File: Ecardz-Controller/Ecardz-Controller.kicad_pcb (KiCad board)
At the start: 4 copper layers, 189 x 115 mm, 169 parts, among them IC1 ST25R3916B-AQWT, IC2 INA180A2IDBVR, J1 MEM2061-01-188-00-A, J10 Conn_01x02, J2 Conn_01x04, J3 Conn_01x05, J4 Conn_01x09, J5 Conn_01x01, J6 Conn_01x24, J7 Conn_01x02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

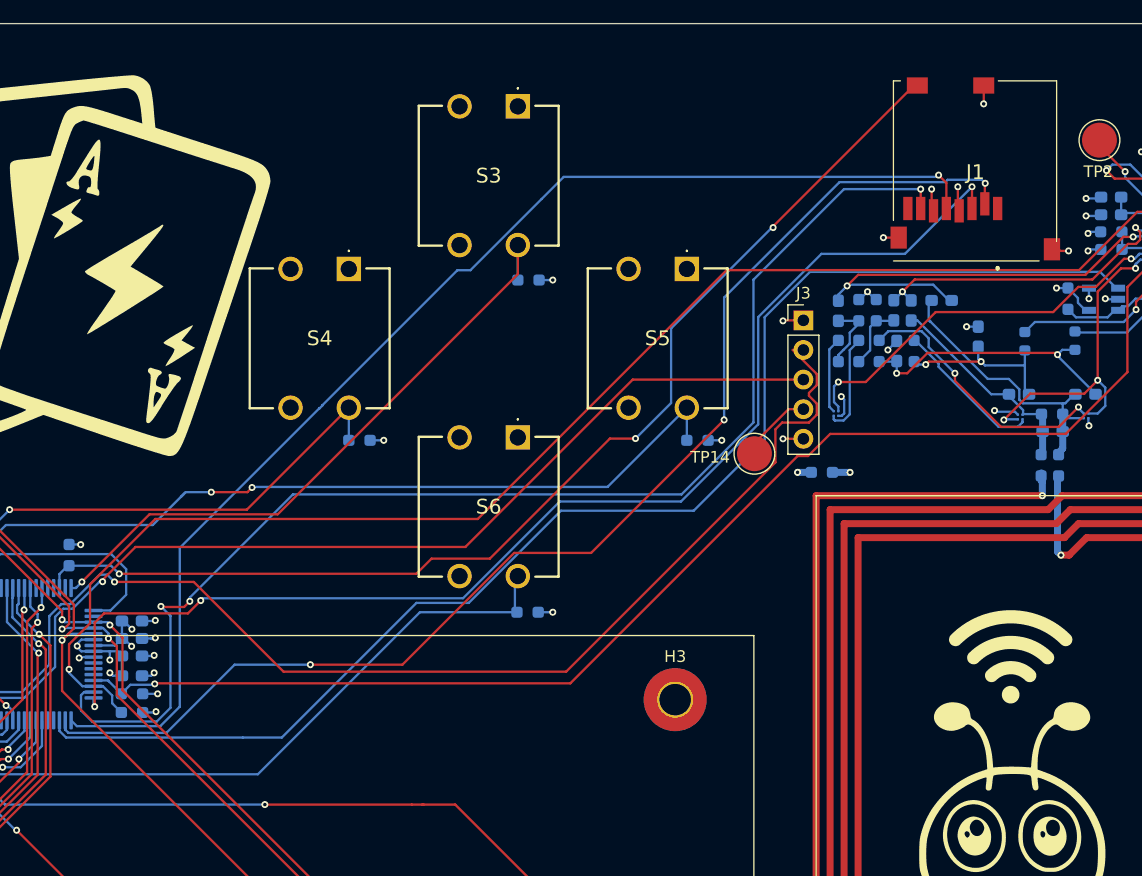
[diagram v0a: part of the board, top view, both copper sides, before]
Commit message: flipped SD card so it enters from card edge
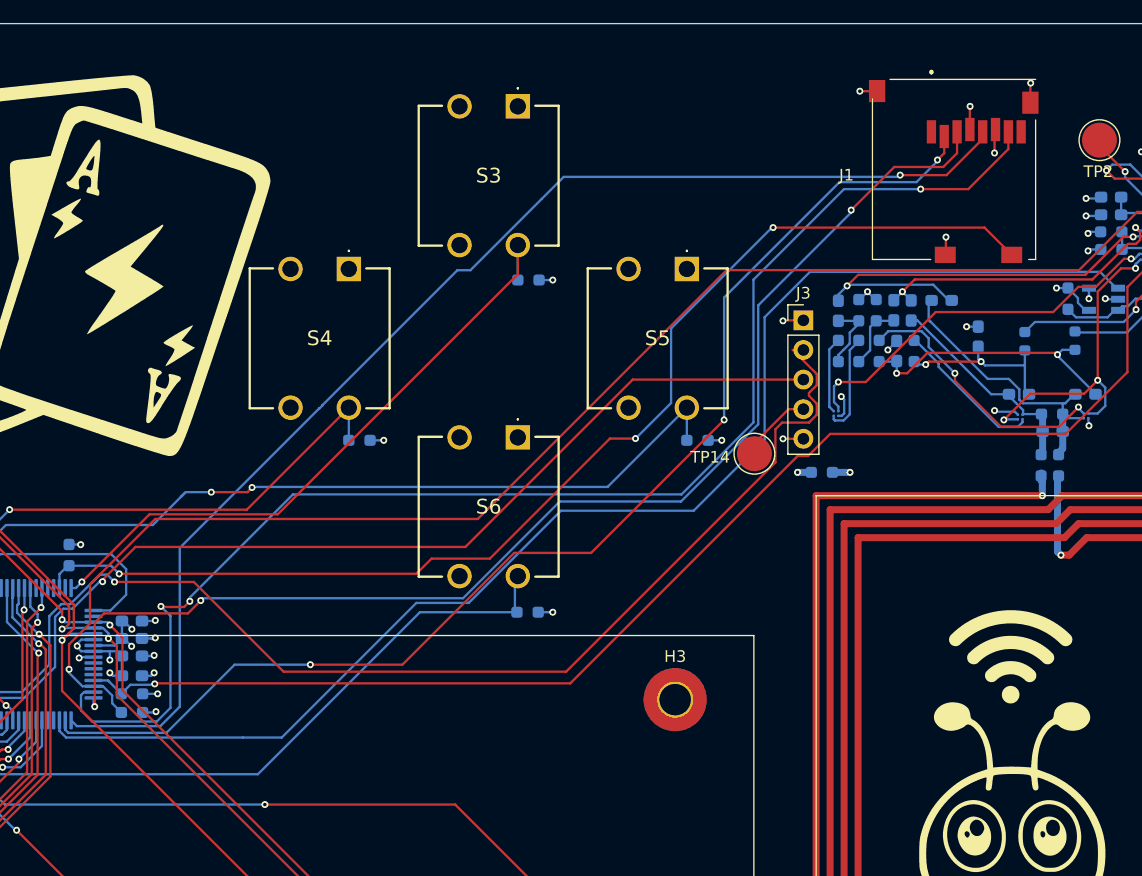
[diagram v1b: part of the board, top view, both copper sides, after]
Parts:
- moved J1 11.7 mm to (205.7, 99.3), turned to 180 degrees
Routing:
- net /MCU/SD_MISO: track 109.2 -> 117.9 mm
- net /MCU/SD_CARD_DETECT: track 96.6 -> 100.7 mm
- net /MCU/SD_SCK: track 104.8 -> 107.9 mm
- net /MCU/SD_CS: track 107.5 -> 104.6 mm
- net /MCU/SD_MOSI: track 105.5 -> 106.6 mm

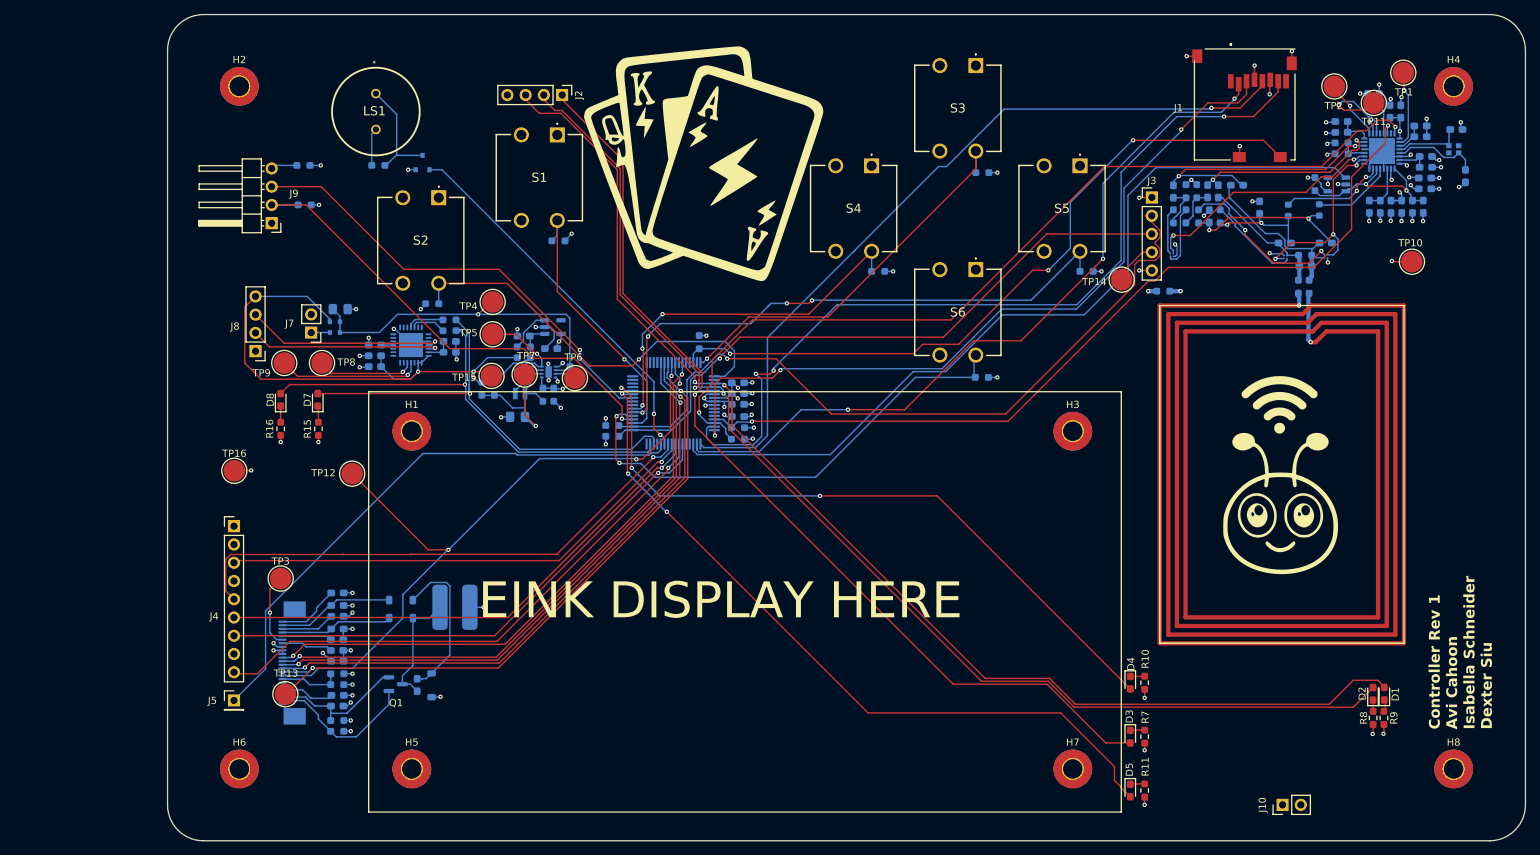
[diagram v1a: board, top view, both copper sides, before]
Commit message: changed headers to 90 degree angled headers
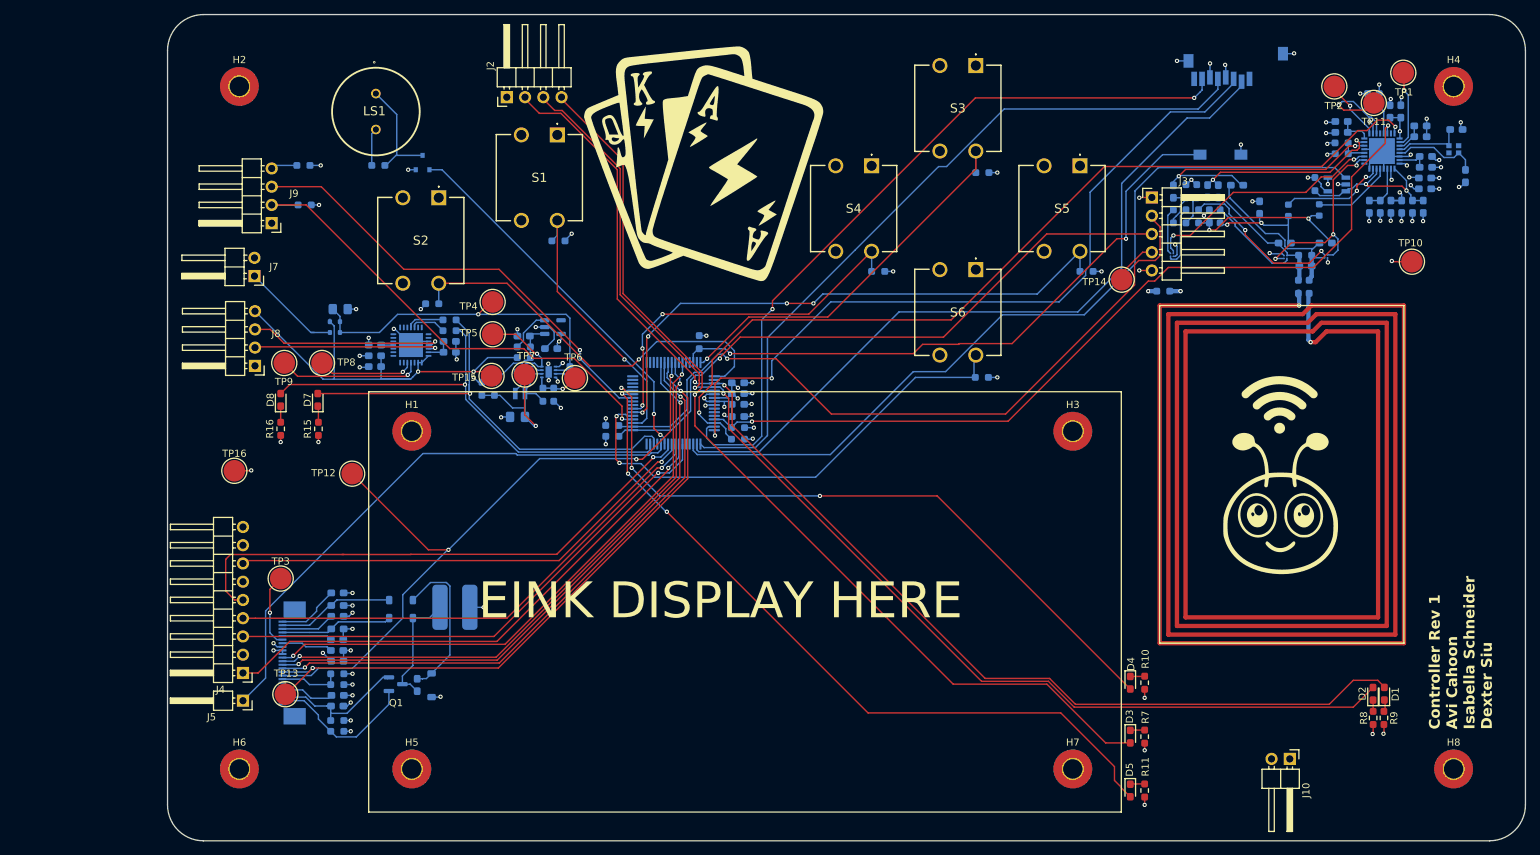
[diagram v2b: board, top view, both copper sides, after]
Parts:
- J1: moved to B.Cu
- J10, J7: footprint Connector_PinHeader_2.54mm:PinHeader_1x02_P2.54mm_Vertical -> Connector_PinHeader_2.54mm:PinHeader_1x02_P2.54mm_Horizontal
- J2, J8: footprint Connector_PinHeader_2.54mm:PinHeader_1x04_P2.54mm_Vertical -> Connector_PinHeader_2.54mm:PinHeader_1x04_P2.54mm_Horizontal
- J3: footprint Connector_PinHeader_2.54mm:PinHeader_1x05_P2.54mm_Vertical -> Connector_PinHeader_2.54mm:PinHeader_1x05_P2.54mm_Horizontal
- J4: footprint Connector_PinHeader_2.54mm:PinHeader_1x09_P2.54mm_Vertical -> Connector_PinHeader_2.54mm:PinHeader_1x09_P2.54mm_Horizontal
- J5: footprint Connector_PinHeader_2.54mm:PinHeader_1x01_P2.54mm_Vertical -> Connector_PinHeader_2.54mm:PinHeader_1x01_P2.54mm_Horizontal
- moved J4 20.5 mm to (60.5, 181.6), turned to 180 degrees
- moved J1 12.8 mm to (192.9, 99.0), turned to 0 degrees
- moved J7 11.2 mm to (62.1, 126.4)
- moved J2 7.71 mm to (97.2, 101.5), turned to 90 degrees
- moved J10 6.48 mm to (206.2, 193.6), turned to -90 degrees
- moved J8 2.05 mm to (62.2, 138.9)
- moved J5 1.25 mm to (60.5, 185.5), turned to 180 degrees
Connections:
- J2 pad 1: /MCU/LED_DEBUG_B -> GND
- J2 pad 2: /MCU/LED_NFC_WORKING -> /MCU/LED_NFC_DONE
- J2 pad 3: /MCU/LED_NFC_DONE -> /MCU/LED_NFC_WORKING
- J2 pad 4: GND -> /MCU/LED_DEBUG_B
- J4 pad 1: +3V3 -> /MCU/SPI_LCD_MISO
- J4 pad 2: GND -> +3V3
- J4 pad 3: /MCU/SPI_LCD_CS -> /MCU/SPI_LCD_SCK
- J4 pad 4: unconnected-(J4-Pin_4-Pad4) -> /MCU/SPI_LCD_MOSI
- J4 pad 6: /MCU/SPI_LCD_MOSI -> unconnected-(J4-Pin_6-Pad6)
- J4 pad 7: /MCU/SPI_LCD_SCK -> /MCU/SPI_LCD_CS
- J4 pad 8: +3V3 -> GND
- J4 pad 9: /MCU/SPI_LCD_MISO -> +3V3
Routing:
- net /MCU/SD_MISO: track 117.9 -> 104.0 mm, vias 3 -> 2
- net /MCU/SD_CARD_DETECT: track 100.7 -> 87.7 mm, vias 3 -> 2
- net /POWER/5V_USBC: track 76.0 -> 63.9 mm
- net /POWER/AUX_POWER: track 2.61 -> 14.1 mm
- net /MCU/SD_SCK: track 107.9 -> 102.3 mm, vias 1 -> 0
- net /MCU/NFC_B_SDA: track 104.1 -> 102.3 mm
- net /MCU/SPI_LCD_MISO: track 76.5 -> 75.1 mm
- net /MCU/SPI_LCD_DC: track 75.1 -> 76.4 mm
- net /MCU/SPI_LCD_SCK: track 74.8 -> 73.6 mm
- net /MCU/SPI_LCD_CS: track 68.4 -> 67.2 mm
- net /MCU/SPI_LCD_MOSI: track 72.3 -> 71.1 mm
- net /MCU/LED_DEBUG_B: track 136.9 -> 135.8 mm
- net /USBC_TO_UART/USBC_D+: track 27.9 -> 27.1 mm
- net /MCU/SD_CS: track 104.6 -> 105.3 mm, vias 3 -> 0
- net /USBC_TO_UART/USBC_D-: track 26.8 -> 26.1 mm
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
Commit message: moved headers to bottom of board, made J3 DNP
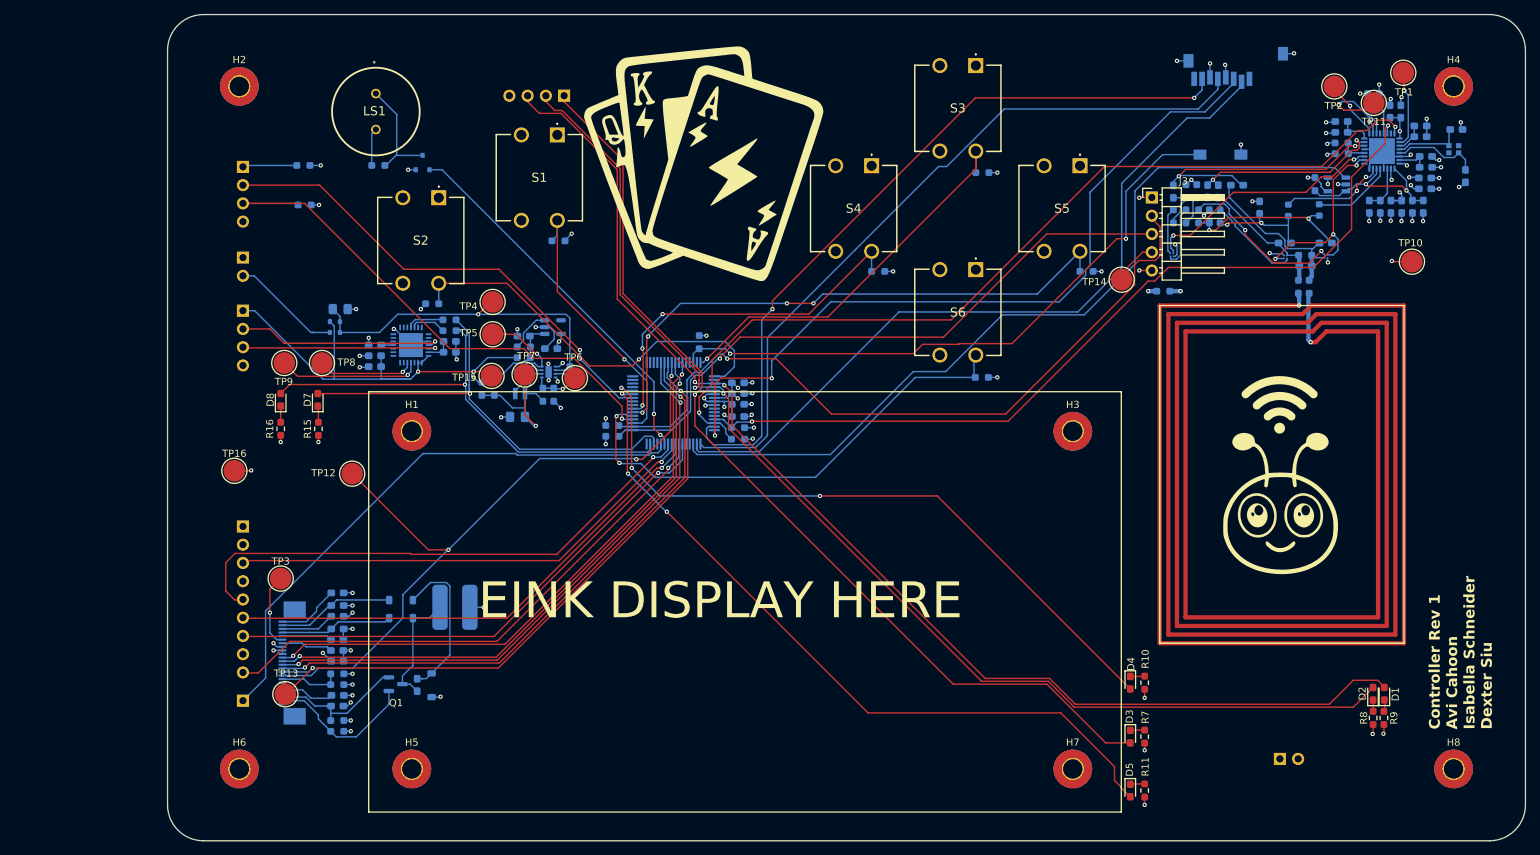
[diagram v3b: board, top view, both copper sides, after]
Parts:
- J10, J2, J4, J5, J7, J8, J9: moved to B.Cu
- moved J4 20.4 mm to (60.5, 161.2)
- moved J9 8.80 mm to (60.5, 111.2)
- moved J2 7.98 mm to (105.2, 101.3)
- moved J8 7.86 mm to (60.5, 131.2)
- moved J7 3.03 mm to (60.5, 123.8)
- moved J10 1.38 mm to (204.8, 193.6)
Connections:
- J10 pad 1: GND -> +3V3
- J10 pad 2: +3V3 -> GND
- J2 pad 1: GND -> /MCU/LED_DEBUG_B
- J2 pad 2: /MCU/LED_NFC_DONE -> /MCU/LED_NFC_WORKING
- J2 pad 3: /MCU/LED_NFC_WORKING -> /MCU/LED_NFC_DONE
- J2 pad 4: /MCU/LED_DEBUG_B -> GND
- J4 pad 1: /MCU/SPI_LCD_MISO -> +3V3
- J4 pad 2: +3V3 -> GND
- J4 pad 3: /MCU/SPI_LCD_SCK -> /MCU/SPI_LCD_CS
- J4 pad 4: /MCU/SPI_LCD_MOSI -> unconnected-(J4-Pin_4-Pad4)
- J4 pad 6: unconnected-(J4-Pin_6-Pad6) -> /MCU/SPI_LCD_MOSI
- J4 pad 7: /MCU/SPI_LCD_CS -> /MCU/SPI_LCD_SCK
- J4 pad 8: GND -> +3V3
- J4 pad 9: +3V3 -> /MCU/SPI_LCD_MISO
- J7 pad 1: /POWER/AUX_POWER -> GND
- J7 pad 2: GND -> /POWER/AUX_POWER
- J8 pad 1: GND -> /POWER/5V_USBC
- J8 pad 2: /USBC_TO_UART/USBC_D- -> /USBC_TO_UART/USBC_D+
- J8 pad 3: /USBC_TO_UART/USBC_D+ -> /USBC_TO_UART/USBC_D-
- J8 pad 4: /POWER/5V_USBC -> GND
- J9 pad 1: +3V3 -> Net-(J9-Pin_1)
- J9 pad 2: /INTERFACE/BUTTON7 -> /MCU/PWR_INDICATOR
- J9 pad 3: /MCU/PWR_INDICATOR -> /INTERFACE/BUTTON7
- J9 pad 4: Net-(J9-Pin_4) -> +3V3
- R12 pad 1: Net-(J9-Pin_4) -> Net-(J9-Pin_1)
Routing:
- net /INTERFACE/BUTTON7: track 67.3 -> 75.5 mm
- net Net-(J9-Pin_1): track 0.00 -> 7.58 mm
- net /MCU/PWR_INDICATOR: track 63.1 -> 67.2 mm
- net Net-(J9-Pin_4): track 3.85 -> 0.00 mm
- net /POWER/5V_USBC: track 63.9 -> 65.6 mm
- net /USBC_TO_UART/USBC_D+: track 27.1 -> 28.8 mm
- net /POWER/AUX_POWER: track 14.1 -> 15.7 mm
- net /USBC_TO_UART/USBC_D-: track 26.1 -> 27.8 mm

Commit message: changed hole positions and fixed flex connector location in 3d model
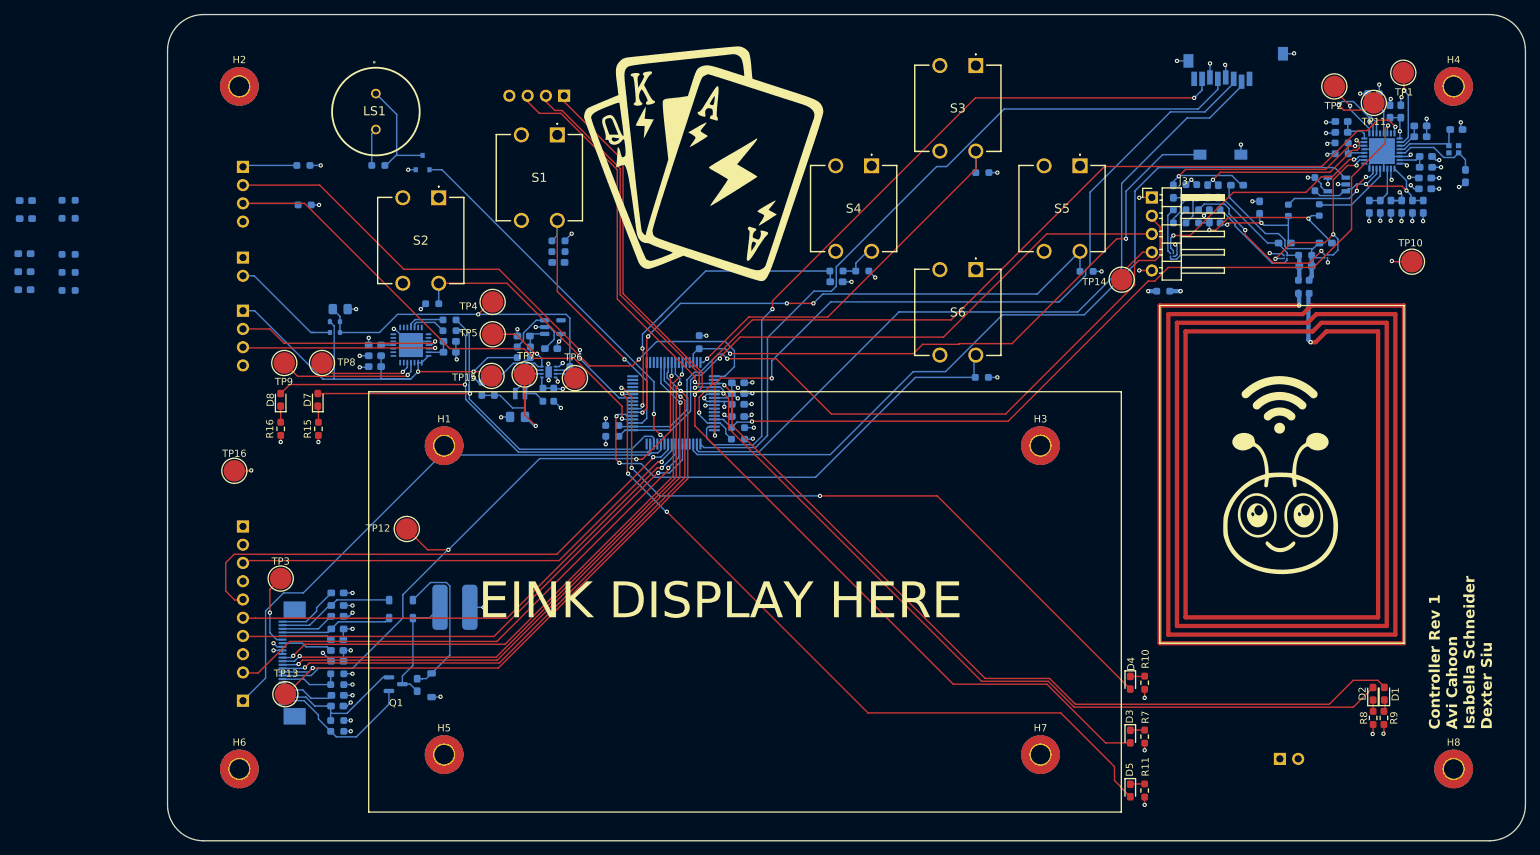
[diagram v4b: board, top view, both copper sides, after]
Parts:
- added C54: 1uF, Capacitor_SMD:C_0603_1608Metric_Pad1.08x0.95mm_HandSolder, B.Cu at (104.4, 124.5)
- added C55: 1uF, Capacitor_SMD:C_0603_1608Metric_Pad1.08x0.95mm_HandSolder, B.Cu at (30.3, 115.9)
- added C56: 1uF, Capacitor_SMD:C_0603_1608Metric_Pad1.08x0.95mm_HandSolder, B.Cu at (30.3, 118.4)
- added C57: 1uF, Capacitor_SMD:C_0603_1608Metric_Pad1.08x0.95mm_HandSolder, B.Cu at (143.1, 127.2)
- added C58: 1uF, Capacitor_SMD:C_0603_1608Metric_Pad1.08x0.95mm_HandSolder, B.Cu at (30.1, 123.3)
- added C59: 1uF, Capacitor_SMD:C_0603_1608Metric_Pad1.08x0.95mm_HandSolder, B.Cu at (30.1, 125.8)
- added C60: 1uF, Capacitor_SMD:C_0603_1608Metric_Pad1.08x0.95mm_HandSolder, B.Cu at (30.1, 128.3)
- added R51: 10k, Resistor_SMD:R_0603_1608Metric_Pad0.98x0.95mm_HandSolder, B.Cu at (104.4, 123.0)
- added R52: 10k, Resistor_SMD:R_0603_1608Metric_Pad0.98x0.95mm_HandSolder, B.Cu at (36.2, 115.8)
- added R53: 10k, Resistor_SMD:R_0603_1608Metric_Pad0.98x0.95mm_HandSolder, B.Cu at (36.2, 118.4)
- added R54: 10k, Resistor_SMD:R_0603_1608Metric_Pad0.98x0.95mm_HandSolder, B.Cu at (143.1, 125.7)
- added R55: 10k, Resistor_SMD:R_0603_1608Metric_Pad0.98x0.95mm_HandSolder, B.Cu at (36.2, 123.4)
- added R56: 10k, Resistor_SMD:R_0603_1608Metric_Pad0.98x0.95mm_HandSolder, B.Cu at (36.2, 125.9)
- added R57: 10k, Resistor_SMD:R_0603_1608Metric_Pad0.98x0.95mm_HandSolder, B.Cu at (36.2, 128.4)
- moved TP12 10.8 mm to (83.3, 161.6)
- moved H1 4.92 mm to (88.5, 150.0)
- moved H3 4.92 mm to (171.5, 150.0)
- moved H5 4.92 mm to (88.5, 193.0)
- moved H7 4.92 mm to (171.5, 193.0)
- moved R23 2.21 mm to (146.7, 125.7)
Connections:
- U1 pad 1: /INTERFACE/BUTTON2 -> /MCU/BUTTON_2
- U1 pad 35: /INTERFACE/BUTTON1 -> /MCU/BUTTON_1
- U1 pad 36: /INTERFACE/BUTTON7 -> /MCU/BUTTON_7
- U1 pad 37: /INTERFACE/BUTTON6 -> /MCU/BUTTON_6
- U1 pad 38: /INTERFACE/BUTTON5 -> /MCU/BUTTON_5
- U1 pad 39: /INTERFACE/BUTTON4 -> /MCU/BUTTON_4
- U1 pad 64: /INTERFACE/BUTTON3 -> /MCU/BUTTON_3
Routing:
- net /INTERFACE/BUTTON4: track 51.9 -> 6.52 mm, vias 3 -> 0
- net /MCU/BUTTON_4: track 0.00 -> 43.2 mm, vias 0 -> 2
- net /INTERFACE/BUSY: track 97.5 -> 86.7 mm
- net /MCU/SD_SCK: track 102.3 -> 103.9 mm
- net GND: track 128.0 -> 129.4 mm, vias 81 -> 82
